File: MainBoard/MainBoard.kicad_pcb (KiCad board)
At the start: 2 copper layers, 150 x 110 mm, 112 parts, among them J1 +12V, J10 SERVO 1, J11 MS SET, J12 STEP, J13 DIR, J14 SERVO2, J15 STEPPER_OUT, J16 ADDL_INPUT1, J17 GND, J18 ADDL_INPUT2, J19 PRESCALER, J2 GND, J3 DOOR_JMPR, J4 HOME, J5 LED, J6 Micro_SD_Card, J7 CENTER TAP, J8 NEUTRAL, J9 LINE, P1 CH0, P2 CH1, P3 CH2, P4 CH3, P5 CH4, P6 CH5, P7 CH6, P8 CH7, Q1 2N7000, Q2 2N7000, U1 MC33167THG, U10 A4988, U2 ESP32-DEVKITC-32U, U3 MCP3204, U4 MCP6004, U5 4051, U6 MCP6004, U7 4051, U8 4051, U9 TMC4210-I, X1 ASE-16MHz

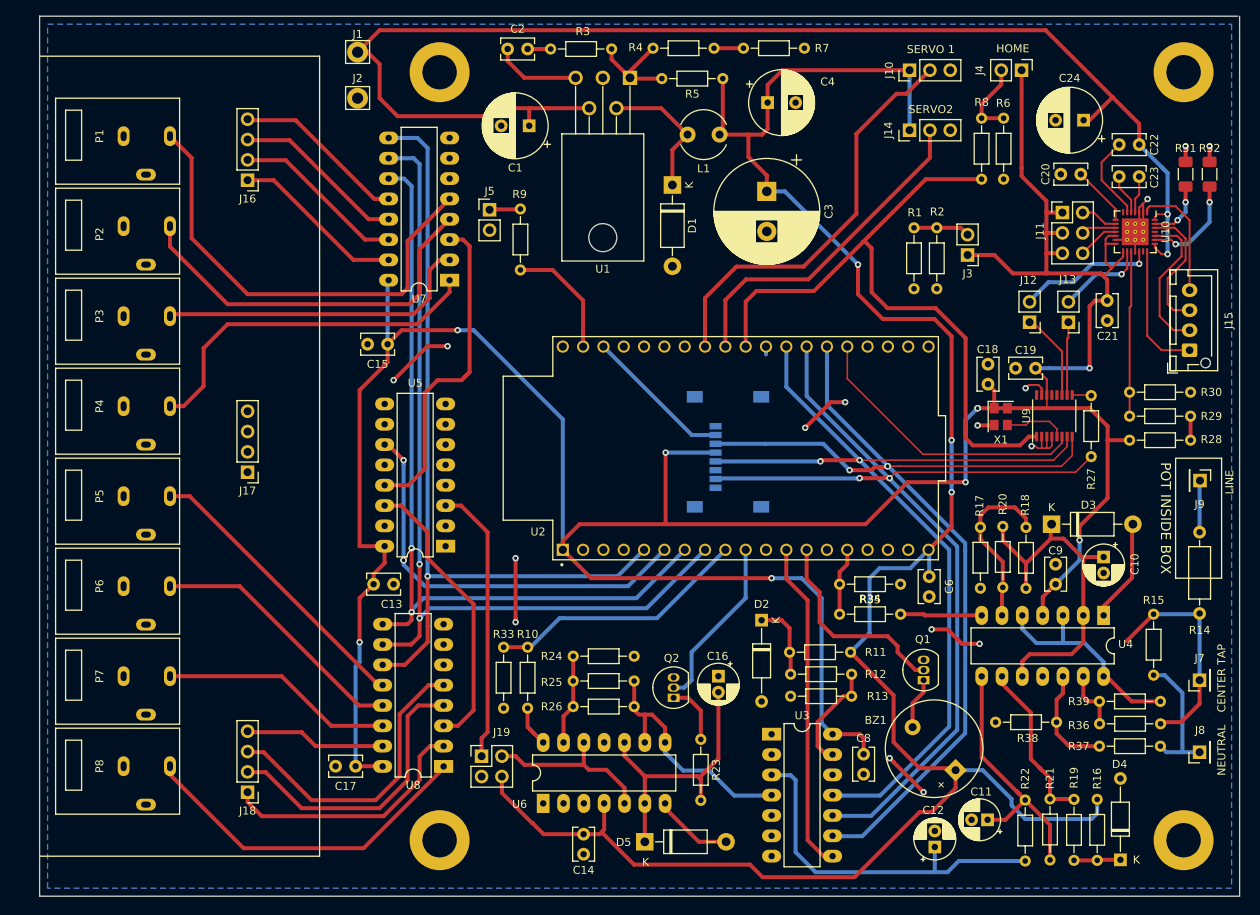
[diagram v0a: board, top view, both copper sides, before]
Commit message: Update Voltage calculation
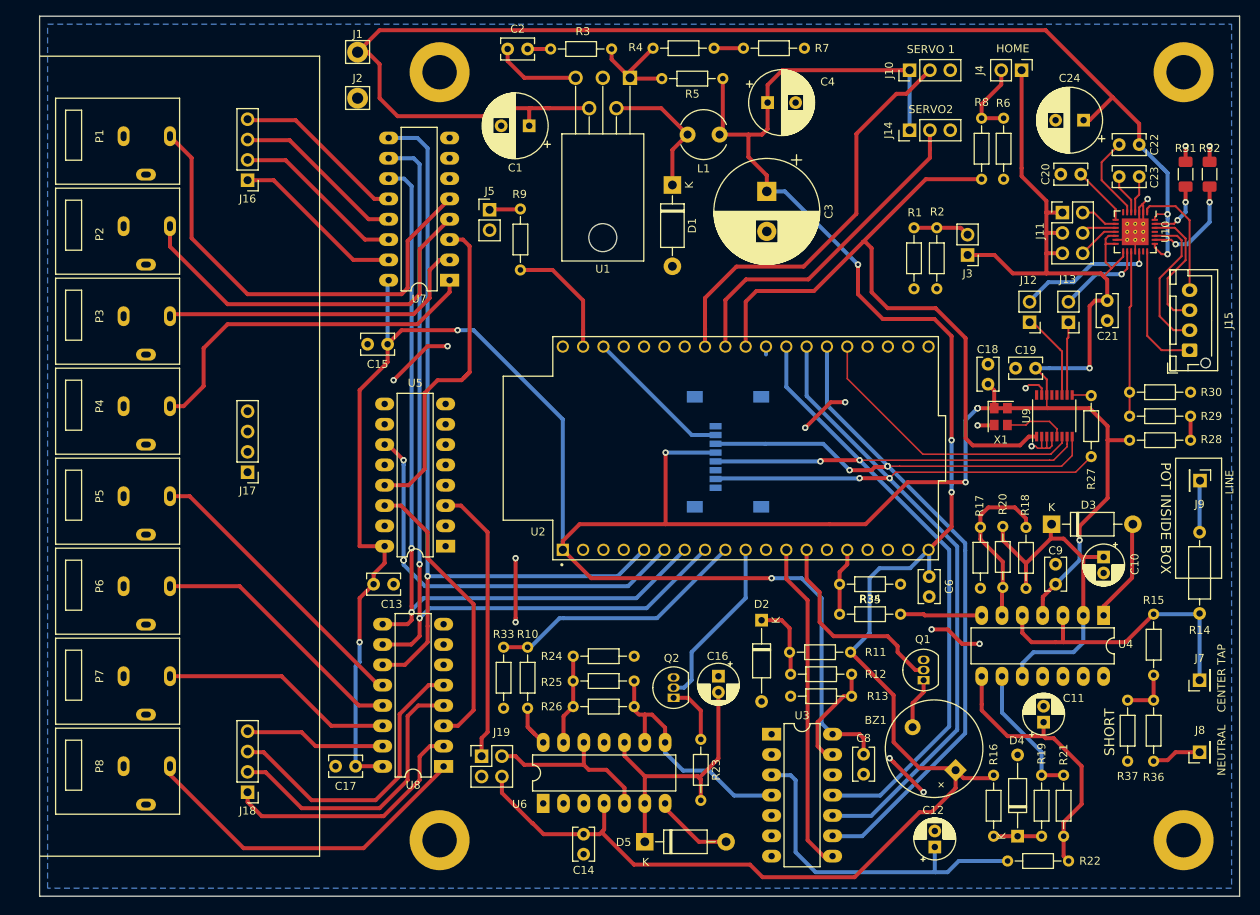
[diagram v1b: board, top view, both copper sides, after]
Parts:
- removed R38, R39: 27k, Resistor_THT:R_Axial_DIN0204_L3.6mm_D1.6mm_P7.62mm_Horizontal
- R14: value 560k -> 680k
- R15: value 10k -> 15k
- R36: value 27k -> 68
- R37: value 27k -> 0
- moved C11 14.1 mm to (201.0, 127.0), turned to 90 degrees
- moved R16 13.3 mm to (194.8, 133.6)
- moved D4 13.2 mm to (197.8, 141.2)
- moved R36 8.21 mm to (214.8, 131.9), turned to 90 degrees
- moved R37 7.06 mm to (211.5, 124.2), turned to 270 degrees
- moved R19 5.05 mm to (200.8, 133.6)
- moved R21 3.42 mm to (203.5, 141.2)
- moved R22 2.20 mm to (196.5, 144.3), turned to 0 degrees
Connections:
- R15 pad 2: /ANALOG_MEASURE/LINE_VOLTAGE_MEASURE/HV_NEUTRAL -> Net-(R15-Pad2)
- R36 pad 1: Net-(R36-Pad1) -> /ANALOG_MEASURE/LINE_VOLTAGE_MEASURE/HV_NEUTRAL
- R36 pad 2: /ANALOG_MEASURE/LINE_VOLTAGE_MEASURE/HV_CNTR_TAP -> Net-(R15-Pad2)
- R37 pad 1: /ANALOG_MEASURE/LINE_VOLTAGE_MEASURE/HV_NEUTRAL -> Net-(R15-Pad2)
- R37 pad 2: Net-(R37-Pad2) -> GND
- U4 pad 12: Net-(R37-Pad2) -> Net-(U4-Pad12)
- U4 pad 13: Net-(R36-Pad1) -> Net-(U4-Pad13)
- U4 pad 14: Net-(R39-Pad1) -> Net-(U4-Pad14)
- U4 pad 3: Net-(R39-Pad1) -> /ANALOG_MEASURE/LINE_VOLTAGE_MEASURE/HV_CNTR_TAP
- U4 pad 5: Net-(R39-Pad1) -> /ANALOG_MEASURE/LINE_VOLTAGE_MEASURE/HV_CNTR_TAP
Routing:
- net Net-(R39-Pad1): track 29.2 -> 0.00 mm
- net +6V: track 259.0 -> 241.7 mm
- net Net-(R37-Pad2): track 15.5 -> 0.00 mm
- net /ANALOG_MEASURE/LINE_VOLTAGE_MEASURE/HV_CNTR_TAP: track 28.0 -> 40.3 mm
- net /ANALOG_MEASURE/LINE_VOLTAGE_MEASURE/HV_NEUTRAL: track 17.1 -> 6.16 mm
- net Net-(R36-Pad1): track 7.62 -> 0.00 mm
- net Net-(R15-Pad2): track 0.00 -> 6.38 mm
- net Net-(R19-Pad1): track 21.3 -> 17.2 mm
- net /ANALOG_MEASURE/LINE_VOLTAGE_MEASURE/LINE_ADC: track 44.8 -> 42.6 mm
- net Net-(C11-Pad1): track 33.0 -> 34.4 mm
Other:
- outline, holes or cut-outs redrawn
- board text added: "SHORT"

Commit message: Final MainBoard
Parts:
- added +3V3: TestPoint_Pad_1.5x1.5mm, TestPoint:TestPoint_Pad_1.5x1.5mm, F.Cu at (154.2, 111.2)
- added +6V: TestPoint_Pad_1.5x1.5mm, TestPoint:TestPoint_Pad_1.5x1.5mm, F.Cu at (177.5, 45.5)
- added MISO: TestPoint_Loop_D2.50mm_Drill1.0mm, TestPoint:TestPoint_Loop_D2.50mm_Drill1.0mm, F.Cu at (171.4, 75.5)
- added MOSI: TestPoint_Loop_D2.50mm_Drill1.0mm, TestPoint:TestPoint_Loop_D2.50mm_Drill1.0mm, F.Cu at (176.2, 75.5)
- added REF**: WEEE-Logo_4.2x6mm_SilkScreen, Symbol:WEEE-Logo_4.2x6mm_SilkScreen, F.Cu at (210.2, 144.5)
- added REF**: Symbol_Highvoltage_Type2_CopperTop_Small, Symbol:Symbol_Highvoltage_Type2_CopperTop_Small, B.Cu at (210.2, 101.8)
- added SCK: TestPoint_Loop_D2.50mm_Drill1.0mm, TestPoint:TestPoint_Loop_D2.50mm_Drill1.0mm, F.Cu at (166.5, 75.5)
- J15: value STEPPER_OUT -> STEPPER
- J3: value DOOR_JMPR -> DOOR
- moved R22 1.40 mm to (196.5, 145.8)
- moved R7 1.27 mm to (172.4, 42.8)
- moved R4 1.20 mm to (161.0, 42.8)
- moved C2 0.10 mm to (134.0, 42.8)
- moved R3 0.10 mm to (147.0, 42.8)
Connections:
- U2 pad 10: /CLR_CURRENT -> /MUX_SELECT1
- U2 pad 11: Net-(U2-Pad11) -> /CLR_CURRENT
- U2 pad 5: /MUX_SELECT2 -> Net-(U2-Pad5)
- U2 pad 6: /MUX_SELECT3 -> /CUR_PHASE
- U2 pad 7: /MUX_SELECT0 -> /MUX_SELECT2
- U2 pad 8: /MUX_SELECT1 -> /MUX_SELECT3
- U2 pad 9: /CUR_PHASE -> /MUX_SELECT0
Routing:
- net /MUX_SELECT3: track 51.8 -> 60.2 mm
- net /MUX_SELECT1: track 107.4 -> 114.7 mm
- net /MUX_SELECT2: track 102.4 -> 109.6 mm
- net /MUX_SELECT0: track 98.6 -> 105.8 mm
- net /SPI0: track 119.1 -> 124.6 mm
- net /SPI2: track 125.8 -> 131.3 mm
- net /SPI1: track 123.1 -> 127.7 mm
- net /CUR_PHASE: track 32.7 -> 30.2 mm, vias 0 -> 1
- net +3V3: track 397.2 -> 399.4 mm
- net Net-(C11-Pad1): track 34.4 -> 35.8 mm
- net /CLR_CURRENT: track 21.7 -> 22.8 mm
- net Net-(R3-Pad1): track 13.6 -> 12.6 mm
- net Net-(U2-Pad28): track 0.98 -> 0.00 mm
- net /ANALOG_MEASURE/LINE_VOLTAGE_MEASURE/LINE_ADC: track 42.6 -> 42.0 mm
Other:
- board text added: "ENSURE 'NEUTRAL' IS CONNECTED TO EARTH GROUND AT PANEL VIA LOW IMPEDANCE PATH"
- board text added: "GROUND ALL SCREWS"
- board text added: "JLCJLCJLCJLC"
- board text added: "PANELIQ MAIN BOARD E-001"
- board text added: "PLACE DAUGHTER BOARD E-003 HERE"
- board text added: "REV A | 2022-02-11 LAYOUT: THOMAS BECKLEY"
